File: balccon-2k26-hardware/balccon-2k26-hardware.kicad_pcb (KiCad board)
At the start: 2 copper layers, 70 x 70 mm, 1 part

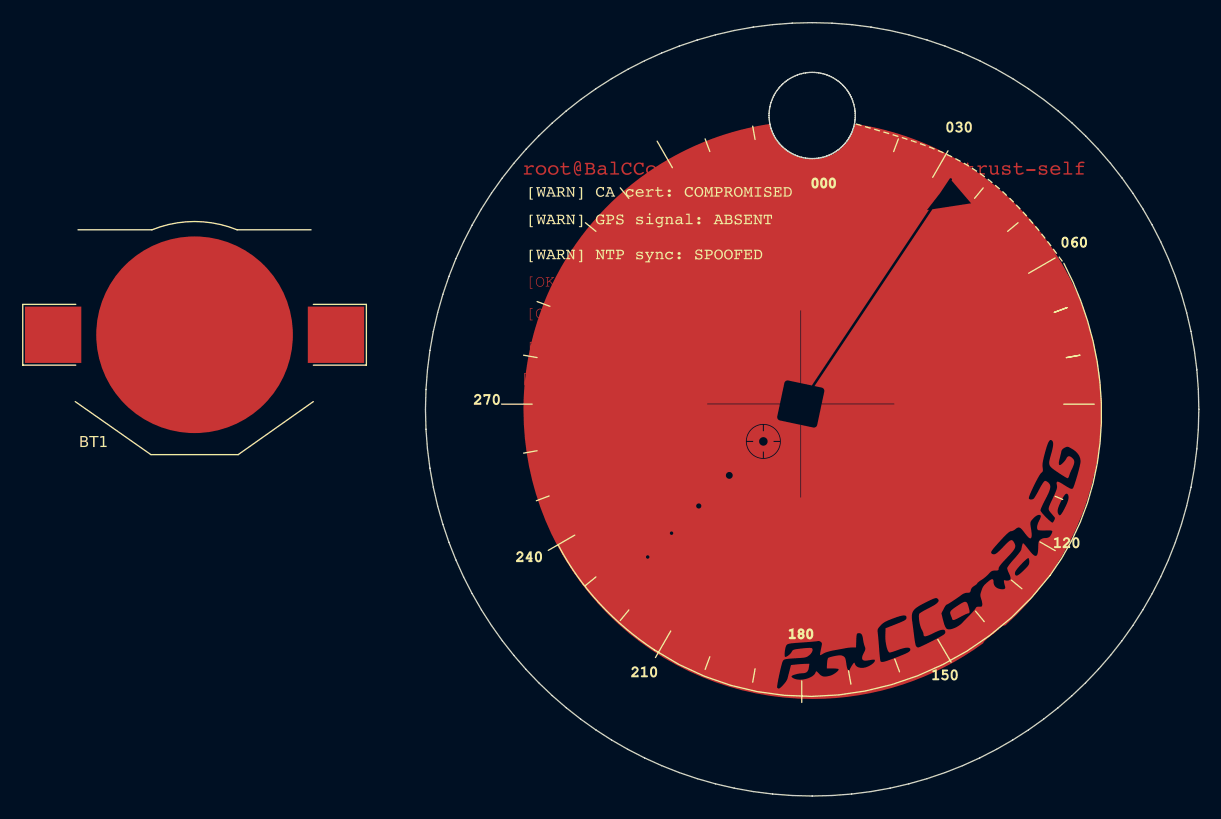
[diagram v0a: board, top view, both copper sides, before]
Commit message: Update schematic/board and add hex, log layer exports
Progress the KiCad schematic and board layout, and export the hex and log
layers alongside the existing ones.

Co-Authored-By: Claude Sonnet 5 <noreply@anthropic.com>
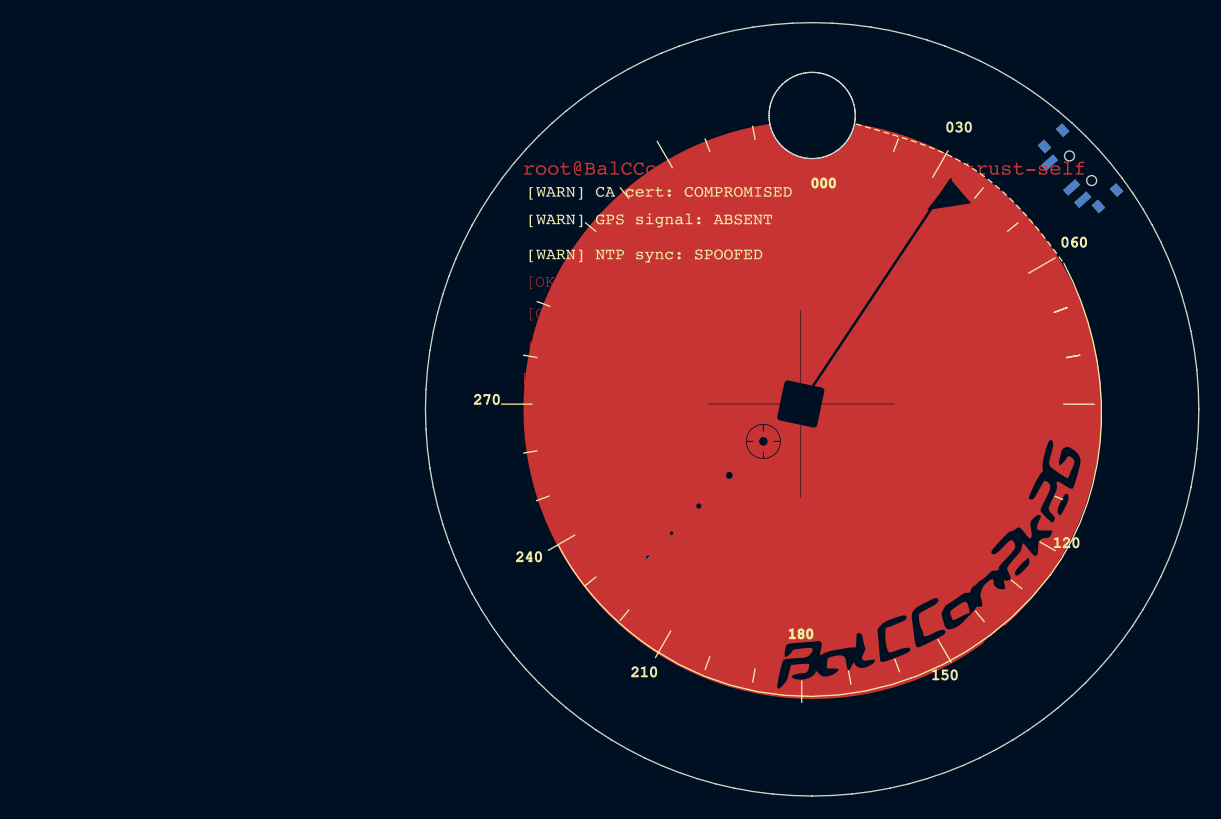
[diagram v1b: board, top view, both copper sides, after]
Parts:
- added D1: 0805, LED_SMD:LED_0805_2012Metric_Pad1.15x1.40mm_HandSolder, B.Cu at (126.7, 92.3)
- added D2: 0603, LED_SMD:LED_0603_1608Metric_Pad1.05x0.95mm_HandSolder, B.Cu at (123.9, 95.1)
- added D3: 0402, LED_SMD:LED_0402_1005Metric_Pad0.77x0.64mm_HandSolder, B.Cu at (121.4, 97.5)
- added D4: 0201, LED_SMD:LED_0201_0603Metric_Pad0.64x0.40mm_HandSolder, B.Cu at (119.2, 99.7)
- added R1: 1k, Resistor_SMD:R_0805_2012Metric_Pad1.20x1.40mm_HandSolder, B.Cu at (131.3, 96.8)
- added R2: 1k, Resistor_SMD:R_0805_2012Metric_Pad1.20x1.40mm_HandSolder, B.Cu at (128.8, 99.5)
- added R3: 1k, Resistor_SMD:R_0805_2012Metric_Pad1.20x1.40mm_HandSolder, B.Cu at (126.3, 102.0)
- added R4: 1k, Resistor_SMD:R_0805_2012Metric_Pad1.20x1.40mm_HandSolder, B.Cu at (123.7, 104.5)
- added SW1: SW_SPDT, Button_Switch_SMD:SW_SPDT_PCM12, B.Cu at (158.2, 64.7)
- BT1: moved to B.Cu
- moved BT1 42.7 mm to (120.8, 76.1), turned to -135 degrees
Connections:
- BT1 pad 1: unconnected-(BT1-+-Pad1) -> Net-(BT1-+)
- BT1 pad 2: unconnected-(BT1---Pad2) -> GND

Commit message: Place all components on the board
Update schematic and board layout with full component placement.

Co-Authored-By: Claude Sonnet 5 <noreply@anthropic.com>
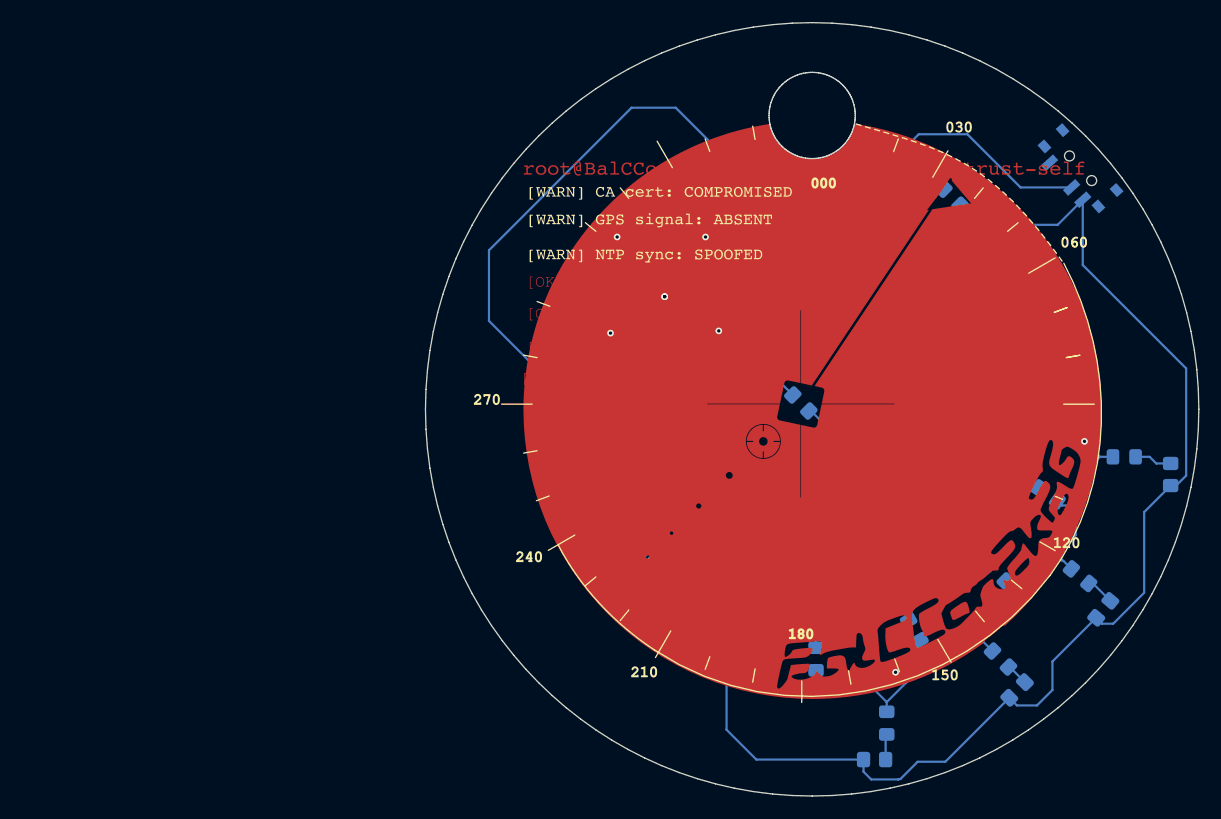
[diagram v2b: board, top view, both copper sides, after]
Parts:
- added D10: 0805, LED_SMD:LED_0805_2012Metric_Pad1.15x1.40mm_HandSolder, B.Cu at (134.5, 108.9)
- added D11: 0805, LED_SMD:LED_0805_2012Metric_Pad1.15x1.40mm_HandSolder, B.Cu at (162.4, 90.6)
- added D12: 0805, LED_SMD:LED_0805_2012Metric_Pad1.15x1.40mm_HandSolder, B.Cu at (158.4, 101.4)
- added D13: 0805, LED_SMD:LED_0805_2012Metric_Pad1.15x1.40mm_HandSolder, B.Cu at (151.2, 108.9)
- added D14: 0805, LED_SMD:LED_0805_2012Metric_Pad1.15x1.40mm_HandSolder, B.Cu at (140.9, 114.7)
- added D5: 0805, LED_SMD:LED_0805_2012Metric_Pad1.15x1.40mm_HandSolder, B.Cu at (146.8, 67.1)
- added D6: 0805, LED_SMD:LED_0805_2012Metric_Pad1.15x1.40mm_HandSolder, B.Cu at (133.1, 85.7)
- added D7: 0805, LED_SMD:LED_0805_2012Metric_Pad1.15x1.40mm_HandSolder, B.Cu at (155.5, 94.0)
- added D8: 0805, LED_SMD:LED_0805_2012Metric_Pad1.15x1.40mm_HandSolder, B.Cu at (150.9, 101.1)
- added D9: 0805, LED_SMD:LED_0805_2012Metric_Pad1.15x1.40mm_HandSolder, B.Cu at (143.4, 106.3)
- added R10: 1k, Resistor_SMD:R_0805_2012Metric_Pad1.20x1.40mm_HandSolder, B.Cu at (134.5, 103.9)
- added R11: 1k, Resistor_SMD:R_0805_2012Metric_Pad1.20x1.40mm_HandSolder, B.Cu at (166.6, 92.2)
- added R12: 1k, Resistor_SMD:R_0805_2012Metric_Pad1.20x1.40mm_HandSolder, B.Cu at (160.5, 104.4)
- added R13: 1k, Resistor_SMD:R_0805_2012Metric_Pad1.20x1.40mm_HandSolder, B.Cu at (152.7, 111.7)
- added R14: 1k, Resistor_SMD:R_0805_2012Metric_Pad1.20x1.40mm_HandSolder, B.Cu at (139.8, 118.0)
- added R5: 1k, Resistor_SMD:R_0805_2012Metric_Pad1.20x1.40mm_HandSolder, B.Cu at (149.7, 70.0)
- added R6: 1k, Resistor_SMD:R_0805_2012Metric_Pad1.20x1.40mm_HandSolder, B.Cu at (136.4, 88.8)
- added R7: 1k, Resistor_SMD:R_0805_2012Metric_Pad1.20x1.40mm_HandSolder, B.Cu at (151.5, 91.4)
- added R8: 1k, Resistor_SMD:R_0805_2012Metric_Pad1.20x1.40mm_HandSolder, B.Cu at (147.8, 97.8)
- added R9: 1k, Resistor_SMD:R_0805_2012Metric_Pad1.20x1.40mm_HandSolder, B.Cu at (140.9, 101.8)
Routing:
- net VCC: track 0.00 -> 161.6 mm
- net GND: track 0.00 -> 129.0 mm, vias 0 -> 8
- net Net-(BT1-+): track 0.00 -> 81.8 mm
- net Net-(D4-A): track 0.00 -> 5.29 mm
- net Net-(D3-A): track 0.00 -> 5.20 mm
- net Net-(D2-A): track 0.00 -> 4.87 mm
- net Net-(D1-A): track 0.00 -> 4.44 mm
- net Net-(D11-A): track 0.00 -> 3.42 mm
- net Net-(D9-A): track 0.00 -> 3.36 mm
- net Net-(D10-A): track 0.00 -> 2.97 mm
- net Net-(D7-A): track 0.00 -> 2.94 mm
- net Net-(D12-A): track 0.00 -> 2.61 mm
- net Net-(D8-A): track 0.00 -> 2.56 mm
- net Net-(D6-A): track 0.00 -> 2.53 mm
- net Net-(D14-A): track 0.00 -> 2.32 mm
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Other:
- board text added: "soldering challenge"
- board text added: "{"
